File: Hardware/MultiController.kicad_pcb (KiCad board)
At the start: 2 copper layers, 80 x 60 mm, 89 parts, among them J1 PC-Fan, J2 USB_C_Receptacle_USB2.0_16P, J3 6P4C, J4 6P4C, J5 6P4C, J6 OLED, J7 6P4C, J8 Screw_Terminal_01x04, Q1 BSS83P, Q3 DMN3008SFG, Q4 AP30P30Q, SW1 RESET, SW2 BOOT, T1 BSS138DW, T2 BSS138DW, T3 BSS138DW, U1 ESP32-S3-WROOM-1, U2 TPS562202, U3 AP2112K-3.3, U4 HUSB238, U5 LM358, U6 LM358

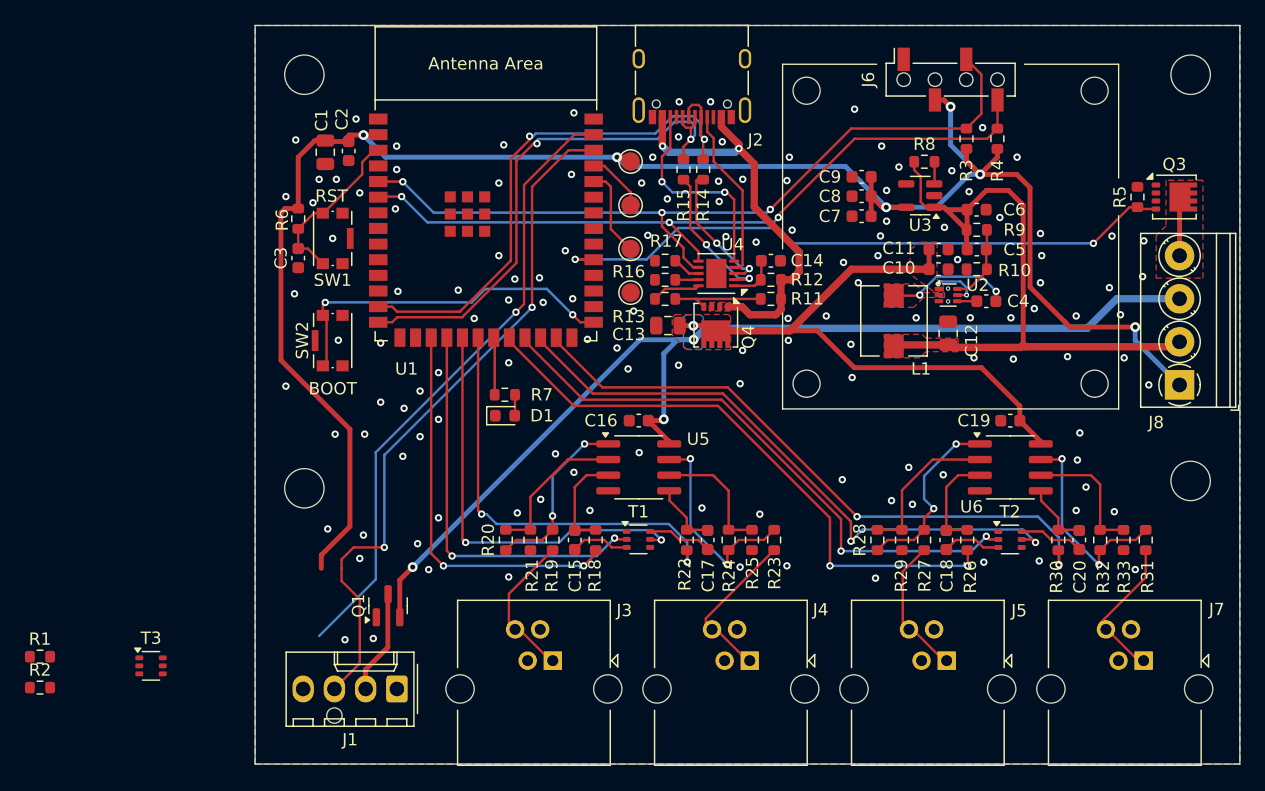
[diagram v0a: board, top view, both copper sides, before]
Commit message: fix #10
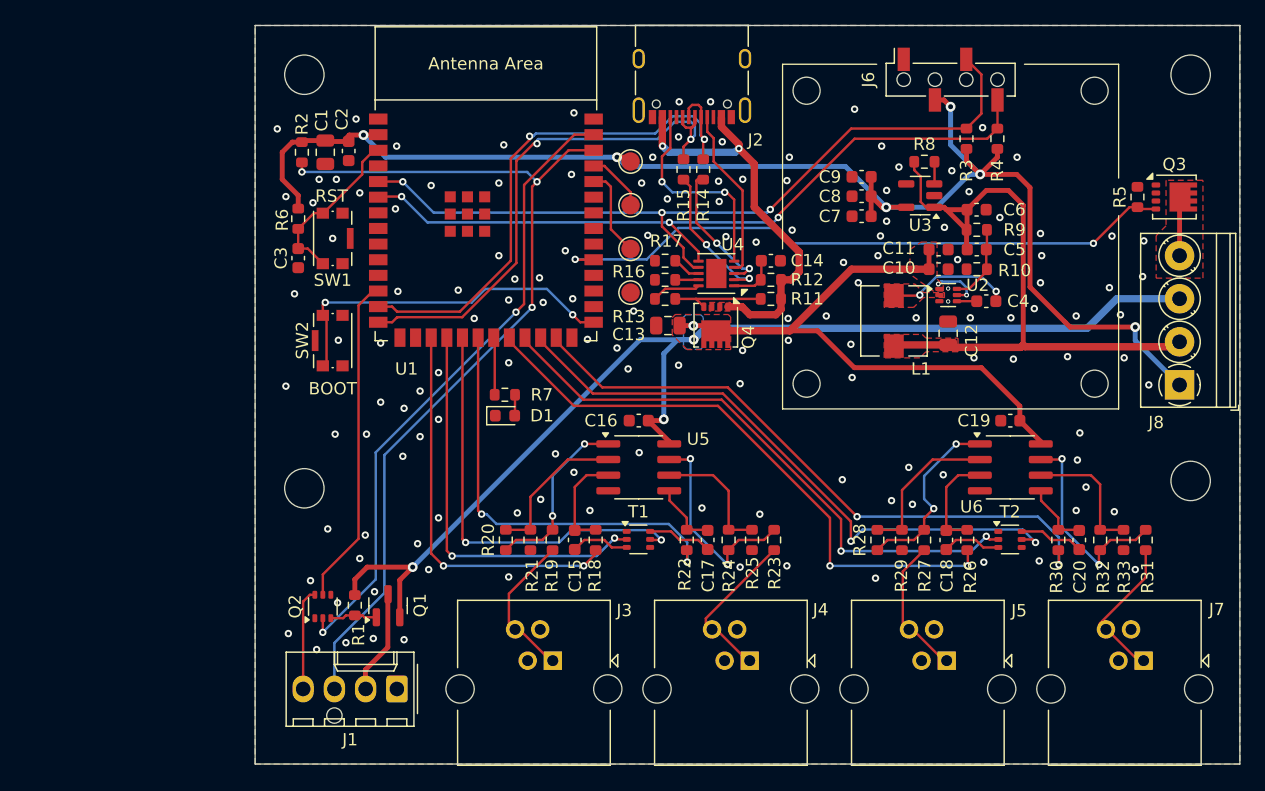
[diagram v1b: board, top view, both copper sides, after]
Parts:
- moved R2 48.4 mm to (64.9, 59.1), turned to -90 degrees
- moved R1 25.9 mm to (69.2, 95.9), turned to -90 degrees
- moved Q2 14.8 mm to (66.6, 96.0), turned to 90 degrees
- renumbered T3 to Q2
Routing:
- net +3V3: track 147.7 -> 116.1 mm
- net /~{FAN_EN}: track 0.00 -> 26.8 mm
- net /Fan_Sense: track 56.4 -> 73.9 mm, vias 2 -> 3
- net Net-(J1-Pin_4): track 0.00 -> 8.28 mm
- net +12V: track 146.6 -> 153.0 mm
- net Net-(Q1-G): track 0.00 -> 3.88 mm
- net /Fan_Ctrl: track 50.9 -> 51.6 mm, vias 1 -> 2
- net GND: vias 136 -> 142

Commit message: changed OP Amps to Rail-to-Rail type fix #8
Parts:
- U5, U6: value LM358 -> TS912
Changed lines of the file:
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@@
 			)
 		)
-		(property "Value" "LM358"
+		(property "Value" "TS912"
 			(at 0 3.4 0)
 			(layer "F.Fab")
@@
 			)
 		)
-		(property "Datasheet" "http://www.ti.com/lit/ds/symlink/lm2904-n.pdf"
+		(property "Datasheet" "www.st.com/resource/en/datasheet/ts912.pdf"
 			(at 0 0 0)
 			(layer "F.Fab")
@@
 			)
 		)
-		(property "Description" "Low-Power, Dual Operational Amplifiers, DIP-8/SOIC-8/TO-99-8"
+		(property "Description" "Dual Rail-to-rail CMOS Operational Amplifier, DIP-8/SOIC-8"
 			(at 0 0 0)
 			(layer "F.Fab")
@@
 			)
 		)
-		(property "Value" "LM358"
+		(property "Value" "TS912"
 			(at 0 3.4 0)
 			(layer "F.Fab")
@@
 			)
 		)
-		(property "Datasheet" "http://www.ti.com/lit/ds/symlink/lm2904-n.pdf"
+		(property "Datasheet" "www.st.com/resource/en/datasheet/ts912.pdf"
 			(at 0 0 0)
 			(layer "F.Fab")
@@
 			)
 		)
-		(property "Description" "Low-Power, Dual Operational Amplifiers, DIP-8/SOIC-8/TO-99-8"
+		(property "Description" "Dual Rail-to-rail CMOS Operational Amplifier, DIP-8/SOIC-8"
 			(at 0 0 0)
 			(layer "F.Fab")

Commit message: fixed references
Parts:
- renumbered T1 to Q5, T2 to Q6
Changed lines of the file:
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@@
 	(net 4 "VBUS")
 	(net 5 "Net-(U5A-+)")
-	(net 6 "Net-(T1A-D1)")
+	(net 6 "Net-(Q5A-D1)")
 	(net 7 "Net-(U5B-+)")
 	(net 8 "Net-(U6A-+)")
@@
 	(net 44 "/ESP32/RX")
 	(net 45 "/ESP32/BOOT0")
-	(net 46 "Net-(T1B-D2)")
-	(net 47 "Net-(T2B-D2)")
-	(net 48 "Net-(T2A-D1)")
+	(net 46 "Net-(Q5B-D2)")
+	(net 47 "Net-(Q6A-D1)")
+	(net 48 "Net-(Q6B-D2)")
 	(net 49 "/ESP32/AUX_EN")
 	(net 50 "+3V3")
@@
 			(layers "F.Cu" "F.Mask" "F.Paste")
 			(roundrect_rratio 0.25)
-			(net 48 "Net-(T2A-D1)")
+			(net 47 "Net-(Q6A-D1)")
 			(pintype "passive")
 		)
@@
 			)
 		)
-		(property "MPN" "LM358DT"
+		(property "MPN" "TS912IDT"
 			(at 0 0 0)
 			(unlocked yes)
@@
 			)
 		)
-		(property "JLCPCB Part #" "C9418"
+		(property "JLCPCB Part #" "C73655"
 			(at 0 0 0)
 			(unlocked yes)
@@
 			(layers "F.Cu" "F.Mask" "F.Paste")
 			(roundrect_rratio 0.25)
-			(net 47 "Net-(T2B-D2)")
+			(net 48 "Net-(Q6B-D2)")
 			(pintype "passive")
 		)
@@
 		(descr "SOT-363, SC-70-6, SC-88")
 		(tags "SOT-363 SC-70-6 SC-88")
-		(property "Reference" "T1"
+		(property "Reference" "Q5"
 			(at 0 -2.25 0)
 			(layer "F.SilkS")
@@
 			(layers "F.Cu" "F.Mask" "F.Paste")
 			(roundrect_rratio 0.25)
-			(net 6 "Net-(T1A-D1)")
+			(net 6 "Net-(Q5A-D1)")
 			(pinfunction "D1")
 			(pintype "passive")
@@
 			(layers "F.Cu" "F.Mask" "F.Paste")
 			(roundrect_rratio 0.25)
-			(net 46 "Net-(T1B-D2)")
+			(net 46 "Net-(Q5B-D2)")
 			(pinfunction "D2")
 			(pintype "passive")
@@
 			(layers "F.Cu" "F.Mask" "F.Paste")
 			(roundrect_rratio 0.25)
-			(net 6 "Net-(T1A-D1)")
+			(net 6 "Net-(Q5A-D1)")
 			(pintype "passive")
 		)
@@
 		(descr "SOT-363, SC-70-6, SC-88")
 		(tags "SOT-363 SC-70-6 SC-88")
-		(property "Reference" "T2"
+		(property "Reference" "Q6"
 			(at 0 -2.25 0)
 			(layer "F.SilkS")
@@
 			(layers "F.Cu" "F.Mask" "F.Paste")
 			(roundrect_rratio 0.25)
-			(net 48 "Net-(T2A-D1)")
+			(net 47 "Net-(Q6A-D1)")
 			(pinfunction "D1")
 			(pintype "passive")
@@
 			(layers "F.Cu" "F.Mask" "F.Paste")
 			(roundrect_rratio 0.25)
-			(net 47 "Net-(T2B-D2)")
+			(net 48 "Net-(Q6B-D2)")
 			(pinfunction "D2")
 			(pintype "passive")
@@
 			)
 		)
-		(property "MPN" "LM358DT"
+		(property "MPN" "TS912IDT"
 			(at 0 0 0)
 			(unlocked yes)
@@
 			)
 		)
-		(property "JLCPCB Part #" "C9418"
+		(property "JLCPCB Part #" "C73655"
 			(at 0 0 0)
 			(unlocked yes)
@@
 			(layers "F.Cu" "F.Mask" "F.Paste")
 			(roundrect_rratio 0.25)
-			(net 46 "Net-(T1B-D2)")
+			(net 46 "Net-(Q5B-D2)")
 			(pintype "passive")
 		)
@@
 	)
 	(segment
-		(start 125.768676 90.6)
-		(end 127.275 90.6)
+		(start 120.255 91.205)
+		(end 119.65 90.6)
 		(width 0.2)
 		(layer "F.Cu")
@@
 	)
 	(segment
-		(start 123.375 89.905)
-		(end 125.073676 89.905)
+		(start 118.025 90.6)
+		(end 117.25 91.375)
 		(width 0.2)
 		(layer "F.Cu")
@@
 	)
 	(segment
-		(start 127.275 90.6)
-		(end 128.05 91.375)
+		(start 119.65 90.6)
+		(end 118.025 90.6)
 		(width 0.2)
 		(layer "F.Cu")
@@
 	)
 	(segment
-		(start 125.073676 89.905)
-		(end 125.768676 90.6)
+		(start 121.475 91.205)
+		(end 120.255 91.205)
 		(width 0.2)
 		(layer "F.Cu")
@@
 	)
 	(segment
-		(start 120.255 91.205)
-		(end 119.65 90.6)
+		(start 125.768676 90.6)
+		(end 127.275 90.6)
 		(width 0.2)
 		(layer "F.Cu")
@@
 	)
 	(segment
-		(start 118.025 90.6)
-		(end 117.25 91.375)
+		(start 123.375 89.905)
+		(end 125.073676 89.905)
 		(width 0.2)
 		(layer "F.Cu")
@@
 	)
 	(segment
-		(start 119.65 90.6)
-		(end 118.025 90.6)
+		(start 127.275 90.6)
+		(end 128.05 91.375)
 		(width 0.2)
 		(layer "F.Cu")
@@
 	)
 	(segment
-		(start 121.475 91.205)
-		(end 120.255 91.205)
+		(start 125.073676 89.905)
+		(end 125.768676 90.6)
 		(width 0.2)
 		(layer "F.Cu")
